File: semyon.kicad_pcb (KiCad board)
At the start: 2 copper layers, 61 x 38.1 mm, 18 parts, among them J1 CR2032 Holder, J2 Conn_01x04, SW1 SW_MEC_5E, SW2 SW_MEC_5E, SW3 SW_MEC_5E, SW4 SW_MEC_5E, SW5 SW_SPDT, U1 STC15F104W

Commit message: REV1.1 - aesthetic changes
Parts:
- moved J2 12.1 mm to (153.0, 96.5)
- moved SW1 0.15 mm to (115.7, 109.2)
- moved SW3 0.15 mm to (158.6, 76.2)
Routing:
- net Net-(J2-Pad2): track 26.1 -> 14.0 mm
- net Net-(J2-Pad3): track 26.6 -> 15.2 mm
- net Net-(J2-Pad1): track 33.6 -> 25.2 mm
- net Net-(R3-Pad2): track 34.8 -> 39.3 mm
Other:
- board text added: "3_3V"
- board text added: "GND"
- board text added: "MCU_RX"
- board text added: "MCU_TX"
- board text added: "SEMYON REV1.1"
- board text removed: "SEMYON REV1.0"
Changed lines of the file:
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@@
   (general
     (thickness 1.6)
-    (drawings 20)
-    (tracks 48)
+    (drawings 24)
+    (tracks 52)
     (zones 0)
     (modules 18)
@@
     (add_net "Net-(D3-Pad1)")
     (add_net "Net-(D4-Pad1)")
+    (add_net "Net-(J2-Pad2)")
     (add_net "Net-(J2-Pad3)")
     (add_net "Net-(R1-Pad2)")
@@
     (add_net "Net-(J1-Pad2)")
     (add_net "Net-(J2-Pad1)")
-    (add_net "Net-(J2-Pad2)")
   )
   (module MountingHole:MountingHole_3.2mm_M3_Pad (layer F.Cu)
@@
   )
   (module Connector_PinHeader_2.54mm:PinHeader_1x04_P2.54mm_Vertical (layer F.Cu)
-    (at 165.1 96.52 180)
+    (at 153.035 96.52 180)
     (descr "Through hole straight pin header, 1x04, 2.54mm pitch, single row")
     (tags "Through hole pin header THT 1x04 2.54mm single row")
@@
   )
   (module Button_Switch_THT:SW_PUSH_6mm (layer F.Cu)
-    (at 115.57 109.22 180)
+    (at 115.72 109.22 180)
     (descr https://www.omron.com/ecb/products/pdf/en-b3f.pdf)
     (tags "tact sw push 6mm")
@@
   )
   (module Button_Switch_THT:SW_PUSH_6mm (layer F.Cu)
-    (at 158.75 76.2)
+    (at 158.6 76.2)
     (descr https://www.omron.com/ecb/products/pdf/en-b3f.pdf)
     (tags "tact sw push 6mm")
@@
     )
   )
+  (gr_text GND (at 156.845 88.9) (layer F.SilkS)
+    (effects (font (size 1 1) (thickness 0.15)))
+  )
+  (gr_text MCU_TX (at 158.115 91.44) (layer F.SilkS)
+    (effects (font (size 1 1) (thickness 0.15)))
+  )
+  (gr_text MCU_RX (at 158.242 93.98) (layer F.SilkS)
+    (effects (font (size 1 1) (thickness 0.15)))
+  )
+  (gr_text 3_3V (at 157.226 96.52) (layer F.SilkS)
+    (effects (font (size 1 1) (thickness 0.15)))
+  )
   (gr_text SEMYON (at 137.16 86.995) (layer F.SilkS)
     (effects (font (size 2.54 3.81) (thickness 0.6)))
   )
-  (gr_text "SEMYON REV1.0" (at 137.16 109.855) (layer F.SilkS)
+  (gr_text "SEMYON REV1.1" (at 137.16 109.855) (layer F.SilkS)
     (effects (font (size 1 1) (thickness 0.15)))
   )
@@
   (segment (start 134.62 98.74) (end 137.16 101.28) (width 0.5) (layer B.Cu) (net 7))
   (segment (start 134.62 76.835) (end 134.62 98.74) (width 0.5) (layer B.Cu) (net 7))
-  (segment (start 159.385 96.52) (end 165.1 96.52) (width 0.5) (layer B.Cu) (net 8))
-  (segment (start 139.7 76.835) (end 159.385 96.52) (width 0.5) (layer B.Cu) (net 8))
+  (segment (start 153.035 96.52) (end 146.05 89.535) (width 0.5) (layer B.Cu) (net 8))
+  (segment (start 146.05 83.185) (end 139.7 76.835) (width 0.5) (layer B.Cu) (net 8))
+  (segment (start 146.05 89.535) (end 146.05 83.185) (width 0.5) (layer B.Cu) (net 8))
   (segment (start 149.86 95.885) (end 139.785 95.885) (width 0.25) (layer F.Cu) (net 9))
-  (segment (start 151.765 93.98) (end 149.86 95.885) (width 0.25) (layer F.Cu) (net 9))
-  (segment (start 165.1 93.98) (end 151.765 93.98) (width 0.25) (layer F.Cu) (net 9))
-  (segment (start 165.1 91.44) (end 163.83 91.44) (width 0.25) (layer F.Cu) (net 10))
-  (segment (start 163.83 91.44) (end 162.56 92.71) (width 0.25) (layer F.Cu) (net 10))
-  (segment (start 162.56 92.71) (end 151.13 92.71) (width 0.25) (layer F.Cu) (net 10))
-  (segment (start 149.225 94.615) (end 139.785 94.615) (width 0.25) (layer F.Cu) (net 10))
-  (segment (start 151.13 92.71) (end 149.225 94.615) (width 0.25) (layer F.Cu) (net 10))
+  (segment (start 153.035 93.98) (end 151.13 95.885) (width 0.25) (layer F.Cu) (net 9))
+  (segment (start 151.13 95.885) (end 149.86 95.885) (width 0.25) (layer F.Cu) (net 9))
+  (segment (start 153.035 91.44) (end 149.86 94.615) (width 0.25) (layer F.Cu) (net 10))
+  (segment (start 149.86 94.615) (end 148.59 94.615) (width 0.25) (layer F.Cu) (net 10))
+  (segment (start 148.59 94.615) (end 139.785 94.615) (width 0.25) (layer F.Cu) (net 10))
+  (segment (start 149.225 94.615) (end 148.59 94.615) (width 0.25) (layer F.Cu) (net 10))
   (segment (start 109.07 100.48) (end 109.22 100.33) (width 0.25) (layer F.Cu) (net 11))
-  (segment (start 109.07 104.72) (end 109.07 100.48) (width 0.25) (layer F.Cu) (net 11))
-  (segment (start 115.57 104.72) (end 109.07 104.72) (width 0.25) (layer F.Cu) (net 11))
   (segment (start 123.19 93.345) (end 120.015 93.345) (width 0.25) (layer F.Cu) (net 11))
   (segment (start 124.46 94.615) (end 123.19 93.345) (width 0.25) (layer F.Cu) (net 11))
@@
   (segment (start 120.015 93.345) (end 113.03 100.33) (width 0.25) (layer F.Cu) (net 11))
   (segment (start 113.03 100.33) (end 109.22 100.33) (width 0.25) (layer F.Cu) (net 11))
-  (segment (start 109.22 85.09) (end 109.22 80.7) (width 0.25) (layer F.Cu) (net 12))
-  (segment (start 109.22 80.7) (end 115.72 80.7) (width 0.25) (layer F.Cu) (net 12))
+  (segment (start 109.22 104.57) (end 109.07 104.72) (width 0.25) (layer B.Cu) (net 11))
+  (segment (start 109.22 100.33) (end 109.22 104.72) (width 0.25) (layer B.Cu) (net 11))
+  (segment (start 115.72 104.72) (end 109.22 104.72) (width 0.25) (layer B.Cu) (net 11))
   (segment (start 112.395 85.09) (end 109.22 85.09) (width 0.25) (layer F.Cu) (net 12))
   (segment (start 122.555 87.63) (end 114.935 87.63) (width 0.25) (layer F.Cu) (net 12))
@@
   (segment (start 127 92.075) (end 122.555 87.63) (width 0.25) (layer F.Cu) (net 12))
   (segment (start 134.535 92.075) (end 127 92.075) (width 0.25) (layer F.Cu) (net 12))
+  (segment (start 115.72 80.7) (end 109.22 80.7) (width 0.25) (layer B.Cu) (net 12))
+  (segment (start 109.22 80.7) (end 109.22 80.645) (width 0.25) (layer B.Cu) (net 12))
+  (segment (start 109.22 80.645) (end 109.22 85.09) (width 0.25) (layer B.Cu) (net 12))
   (segment (start 165.25 84.94) (end 165.1 85.09) (width 0.25) (layer B.Cu) (net 13))
-  (segment (start 165.25 80.7) (end 165.25 84.94) (width 0.25) (layer B.Cu) (net 13))
-  (segment (start 147.955 92.075) (end 158.75 80.7) (width 0.25) (layer F.Cu) (net 13))
-  (segment (start 139.785 92.075) (end 147.955 92.075) (width 0.25) (layer F.Cu) (net 13))
-  (segment (start 158.75 80.7) (end 165.25 80.7) (width 0.25) (layer F.Cu) (net 13))
-  (segment (start 165.1 104.72) (end 165.1 100.33) (width 0.25) (layer F.Cu) (net 14))
+  (segment (start 165.1 85.09) (end 163.195 86.995) (width 0.25) (layer F.Cu) (net 13))
+  (segment (start 163.195 86.995) (end 151.765 86.995) (width 0.25) (layer F.Cu) (net 13))
+  (segment (start 146.685 92.075) (end 139.785 92.075) (width 0.25) (layer F.Cu) (net 13))
+  (segment (start 151.765 86.995) (end 146.685 92.075) (width 0.25) (layer F.Cu) (net 13))
+  (segment (start 165.25 80.7) (end 158.75 80.7) (width 0.25) (layer B.Cu) (net 13))
+  (segment (start 165.1 80.7) (end 165.1 85.09) (width 0.25) (layer B.Cu) (net 13))
   (segment (start 138.96 93.345) (end 137.16 95.145) (width 0.25) (layer F.Cu) (net 14))
   (segment (start 139.785 93.345) (end 138.96 93.345) (width 0.25) (layer F.Cu) (net 14))
@@
   (segment (start 163.195 98.425) (end 165.1 100.33) (width 0.25) (layer F.Cu) (net 14))
   (segment (start 139.065 98.425) (end 163.195 98.425) (width 0.25) (layer F.Cu) (net 14))
-  (segment (start 165.1 104.72) (end 158.6 104.72) (width 0.25) (layer F.Cu) (net 14))
+  (segment (start 158.6 104.72) (end 165.1 104.72) (width 0.25) (layer B.Cu) (net 14))
+  (segment (start 165.1 104.72) (end 165.1 100.33) (width 0.25) (layer B.Cu) (net 14))
   (zone (net 1) (net_name "Net-(C1-Pad1)") (layer F.Cu) (hatch edge 0.508)
     (connect_pads (clearance 0.508))

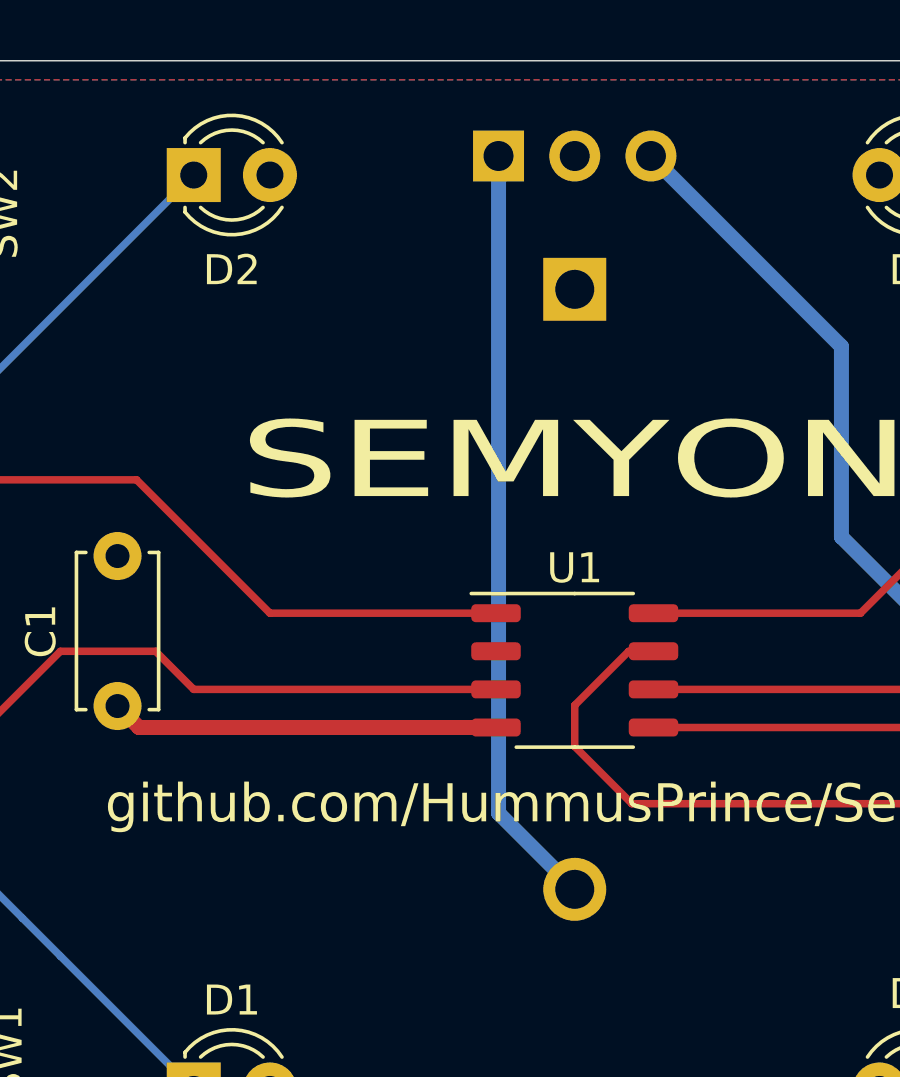
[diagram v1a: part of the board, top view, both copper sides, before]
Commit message: minor power trace modification to REV1.1
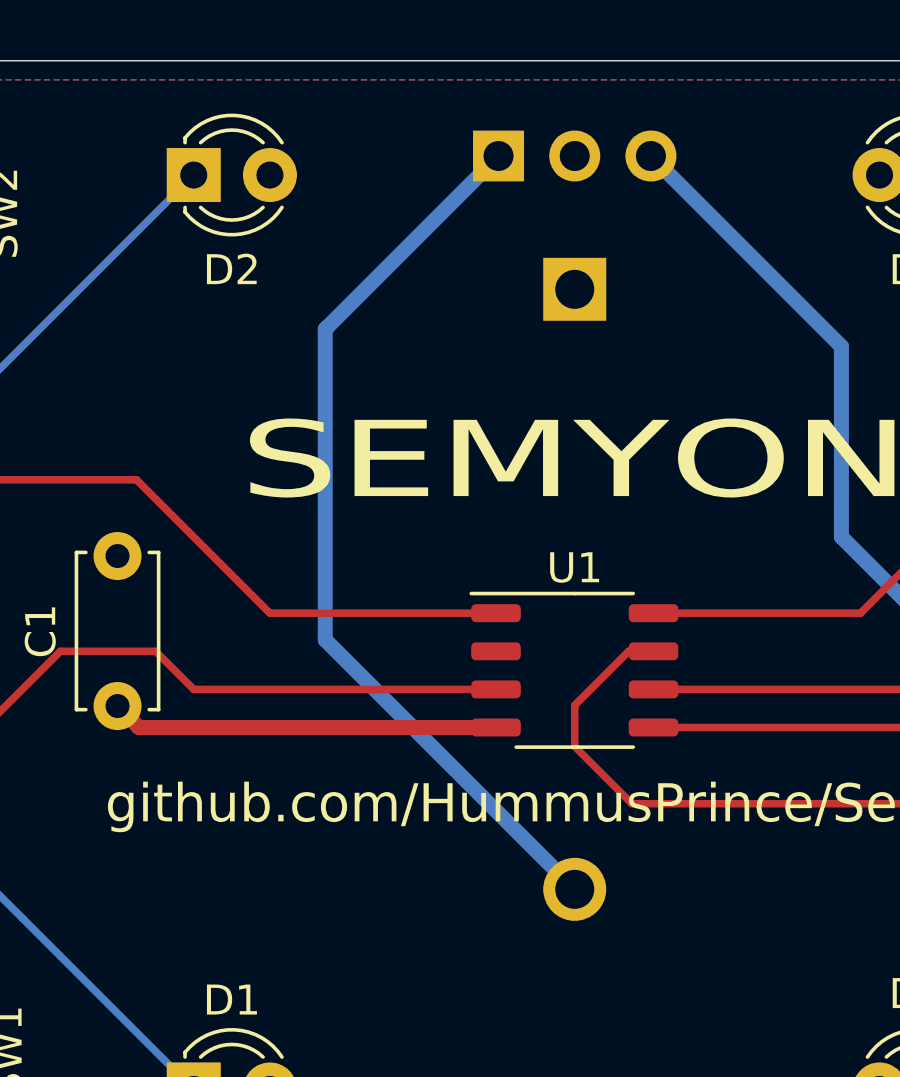
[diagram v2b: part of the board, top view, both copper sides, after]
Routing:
- net Net-(J1-Pad2): track 25.5 -> 30.3 mm
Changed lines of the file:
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@@
     (thickness 1.6)
     (drawings 24)
-    (tracks 52)
+    (tracks 54)
     (zones 0)
     (modules 18)
@@
   (segment (start 157.48 85.09) (end 149.86 77.47) (width 0.25) (layer B.Cu) (net 5))
   (segment (start 157.48 100.33) (end 149.86 107.95) (width 0.25) (layer B.Cu) (net 6))
-  (segment (start 134.62 98.74) (end 137.16 101.28) (width 0.5) (layer B.Cu) (net 7))
-  (segment (start 134.62 76.835) (end 134.62 98.74) (width 0.5) (layer B.Cu) (net 7))
+  (segment (start 134.62 76.835) (end 128.905 82.55) (width 0.5) (layer B.Cu) (net 7))
+  (segment (start 137.16 101.28) (end 128.844 92.964) (width 0.5) (layer B.Cu) (net 7))
+  (segment (start 128.844 82.611) (end 128.905 82.55) (width 0.5) (layer B.Cu) (net 7))
+  (segment (start 128.844 92.964) (end 128.844 82.611) (width 0.5) (layer B.Cu) (net 7))
   (segment (start 153.035 96.52) (end 146.05 89.535) (width 0.5) (layer B.Cu) (net 8))
   (segment (start 146.05 83.185) (end 139.7 76.835) (width 0.5) (layer B.Cu) (net 8))

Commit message: cosmetic changes
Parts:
- moved C1 0.51 mm to (121.4, 90.2)
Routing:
- net GND: track 12.9 -> 13.4 mm

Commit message: Rev 1.2, created+added correct battery holder
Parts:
- J1: footprint Battery:BatteryHolder_ComfortableElectronic_CH273-2450_1x2450 -> semyon:BatteryHolder_CR2032
- moved J1 12.7 mm to (137.2, 94.0), turned to 180 degrees
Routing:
- net Net-(J1-Pad2): track 30.3 -> 31.6 mm
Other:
- board text added: "SEMYON REV1.2"
- board text removed: "SEMYON REV1.1"

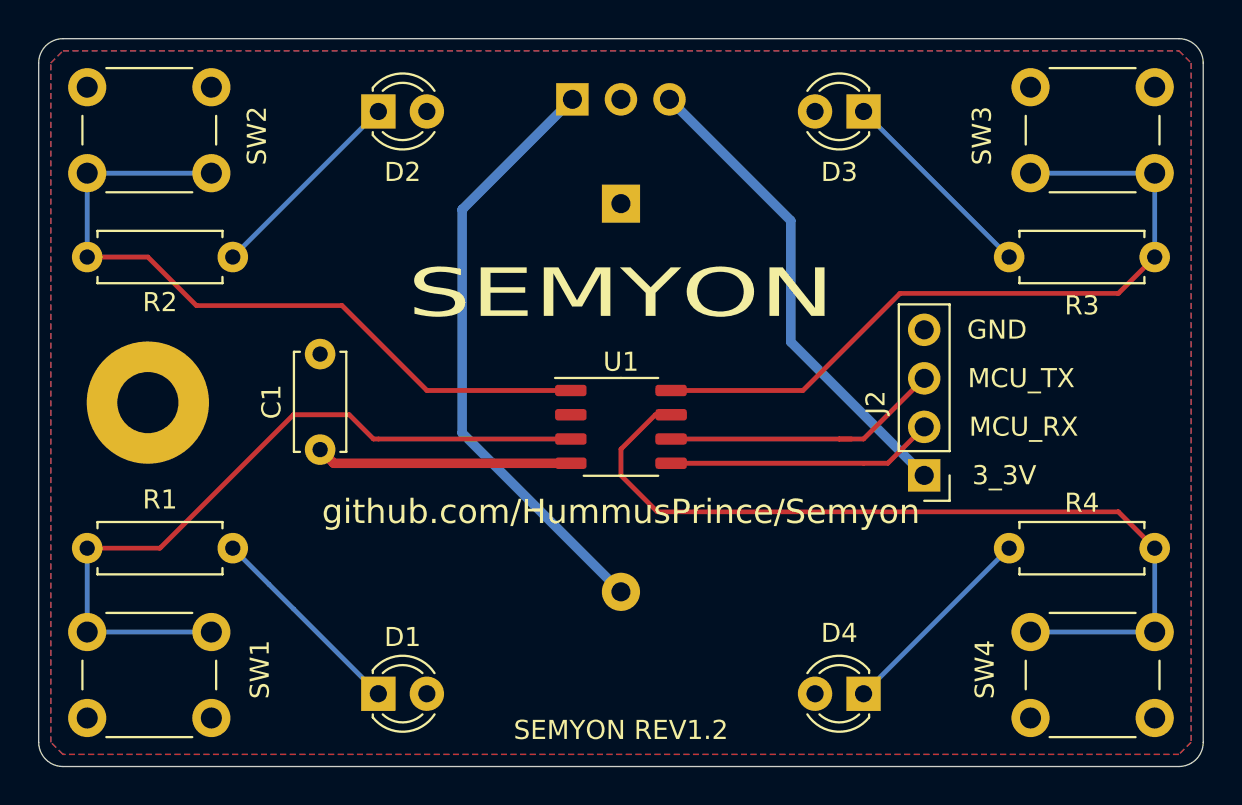
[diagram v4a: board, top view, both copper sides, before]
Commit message: Rev 2.0, board resized to fit CR2032
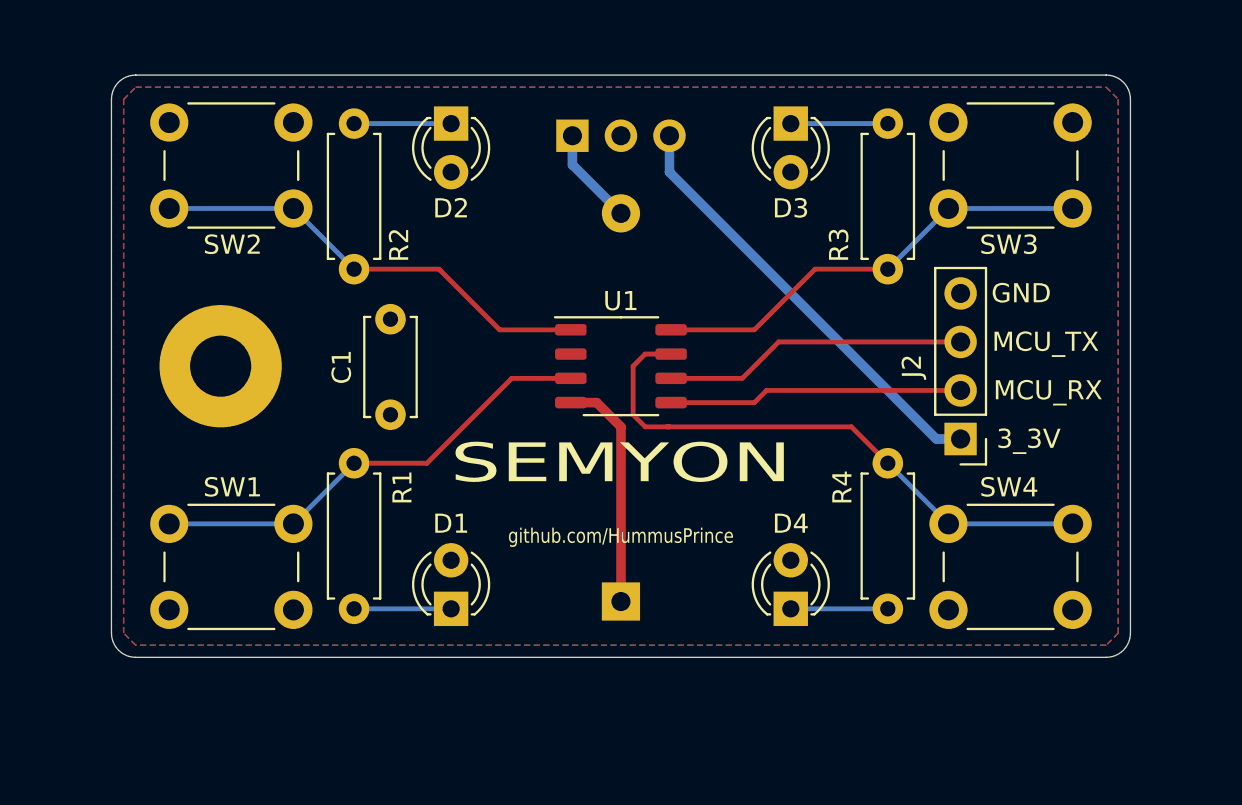
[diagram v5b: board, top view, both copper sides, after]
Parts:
- moved R2 9.44 mm to (123.2, 78.1), turned to 270 degrees
- moved R3 9.44 mm to (151.1, 78.1), turned to 270 degrees
- moved SW1 7.11 mm to (120.0, 103.6)
- moved SW4 7.11 mm to (160.8, 103.6)
- moved R1 7.10 mm to (123.2, 103.5), turned to 90 degrees
- moved R4 7.10 mm to (151.1, 103.5), turned to 90 degrees
- moved D1 5.85 mm to (128.3, 103.5), turned to 90 degrees
- moved D4 5.85 mm to (146.1, 103.5), turned to 90 degrees
- moved SW2 4.68 mm to (113.5, 78.0)
- moved SW3 4.68 mm to (154.3, 78.0)
- moved REF** 4.26 mm to (116.2, 90.8)
- moved C1 4.11 mm to (125.1, 88.3)
- moved D2 3.86 mm to (128.3, 78.1), turned to 270 degrees
- moved D3 3.86 mm to (146.1, 78.1), turned to 270 degrees
- moved U1 3.17 mm to (137.2, 90.8)
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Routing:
- net Net-(J1-Pad2): track 31.6 -> 5.12 mm
- net Net-(R1-Pad2): track 40.0 -> 24.2 mm
- net Net-(R3-Pad2): track 39.3 -> 23.7 mm
- net Net-(R2-Pad2): track 39.2 -> 23.7 mm
- net Net-(R4-Pad2): track 45.2 -> 30.3 mm
- net Net-(D4-Pad1): track 10.8 -> 5.08 mm
- net Net-(D3-Pad1): track 10.8 -> 5.08 mm
- net Net-(D2-Pad1): track 10.8 -> 5.08 mm
- net Net-(D1-Pad1): track 10.8 -> 5.08 mm
- net Net-(J2-Pad1): track 25.2 -> 22.9 mm
- net Net-(J2-Pad2): track 14.0 -> 15.4 mm
- net GND: track 13.4 -> 12.3 mm
- net Net-(J2-Pad3): track 15.2 -> 15.9 mm
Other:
- board size 61 x 38.1 mm -> 53.3 x 30.5 mm
- board text added: "SEMYON REV2.0"
- board text added: "github.com/HummusPrince"
- board text removed: "SEMYON REV1.2"
- board text removed: "github.com/HummusPrince/Semyon"
